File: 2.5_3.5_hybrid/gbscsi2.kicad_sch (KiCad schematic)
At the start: 120 parts, among them J1 Conn_01x02, J2 TF003, J4 Conn_01x04, J5 SCSI_50-2P_2mm, J6 SCSI_50P_2.54mm, Q1 AO3401A, Q10 AO3401A, Q11 AO3401A, Q12 AO3401A, Q13 AO3401A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

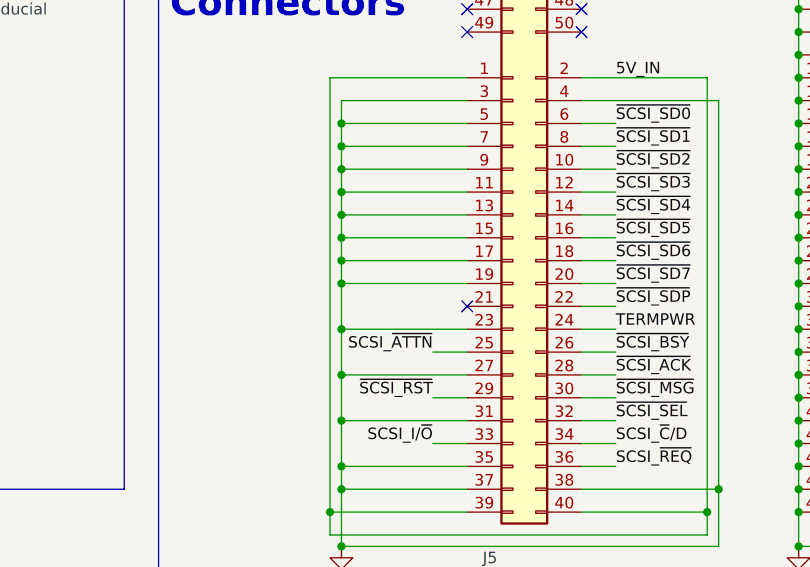
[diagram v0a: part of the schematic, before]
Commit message: Changed diodes in BoM, minor corrections to PCB, documentation
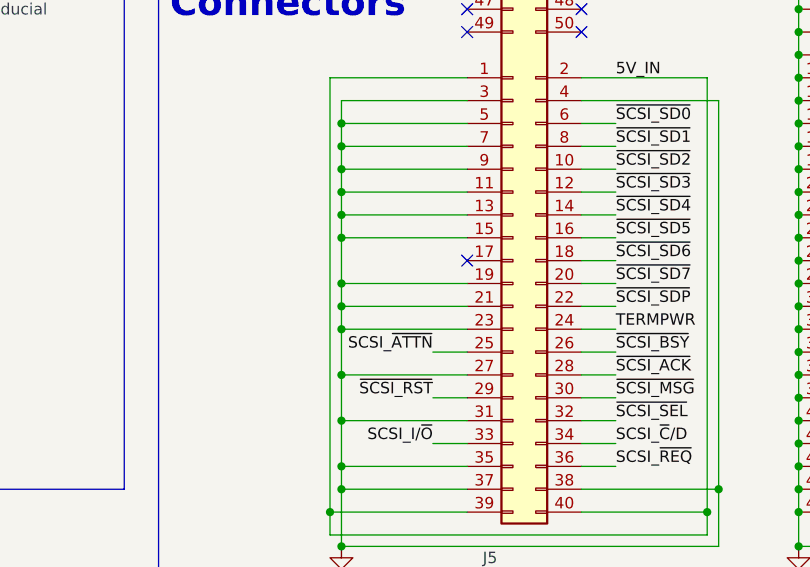
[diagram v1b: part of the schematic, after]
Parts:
- D? (x4): LCSC C8598 -> C82544
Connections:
- net GND: now also J5.21 (Pin_21); no longer J5.17 (Pin_17)
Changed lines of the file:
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@@
   (junction (at 187.96 77.47) (diameter 0) (color 0 0 0 0)
   )
+  (junction (at 320.04 57.15) (diameter 0) (color 0 0 0 0)
+  )
   (junction (at 384.81 59.69) (diameter 0) (color 0 0 0 0)
   )
@@
   (junction (at 328.93 158.75) (diameter 0) (color 0 0 0 0)
   )
-  (junction (at 320.04 52.07) (diameter 0) (color 0 0 0 0)
-  )
   (junction (at 370.84 77.47) (diameter 0) (color 0 0 0 0)
   )
@@
   (no_connect (at 346.71 21.59))
   (no_connect (at 54.61 77.47))
+  (no_connect (at 334.01 52.07))
   (no_connect (at 334.01 24.13))
   (no_connect (at 76.2 34.29))
   (no_connect (at 148.59 35.56))
-  (no_connect (at 334.01 57.15))
   (no_connect (at 334.01 21.59))
   (no_connect (at 76.2 31.75))
@@
     (stroke (width 0) (type default))
   )
+  (wire (pts (xy 320.04 57.15) (xy 334.01 57.15))
+    (stroke (width 0) (type default))
+  )
   (wire (pts (xy 370.84 49.53) (xy 370.84 52.07))
     (stroke (width 0) (type default))
@@
     (stroke (width 0) (type default))
   )
+  (wire (pts (xy 320.04 57.15) (xy 320.04 59.69))
+    (stroke (width 0) (type default))
+  )
   (wire (pts (xy 74.93 54.61) (xy 77.47 54.61))
     (stroke (width 0) (type default))
@@
     (stroke (width 0) (type default))
   )
-  (wire (pts (xy 320.04 52.07) (xy 334.01 52.07))
-    (stroke (width 0) (type default))
-  )
   (wire (pts (xy 193.04 200.66) (xy 193.04 198.12))
     (stroke (width 0) (type default))
@@
     (stroke (width 0) (type default))
   )
-  (wire (pts (xy 320.04 49.53) (xy 320.04 52.07))
-    (stroke (width 0) (type default))
-  )
   (wire (pts (xy 36.83 54.61) (xy 39.37 54.61))
     (stroke (width 0) (type default))
@@
     (stroke (width 0) (type default))
   )
-  (wire (pts (xy 320.04 52.07) (xy 320.04 54.61))
+  (wire (pts (xy 320.04 49.53) (xy 320.04 54.61))
     (stroke (width 0) (type default))
   )
-  (wire (pts (xy 320.04 54.61) (xy 320.04 59.69))
+  (wire (pts (xy 320.04 54.61) (xy 320.04 57.15))
     (stroke (width 0) (type default))
   )
@@
       (effects (font (size 1.27 1.27)))
     )
-    (property "LCSC" "C8598" (at 171.45 27.94 0)
+    (property "LCSC" "C82544" (at 171.45 27.94 0)
       (effects (font (size 1.27 1.27)) hide)
     )
@@
       (effects (font (size 1.27 1.27)))
     )
-    (property "LCSC" "C8598" (at 163.83 35.56 0)
+    (property "LCSC" "C82544" (at 163.83 35.56 0)
       (effects (font (size 1.27 1.27)) hide)
     )
@@
       (effects (font (size 1.27 1.27)))
     )
-    (property "LCSC" "C8598" (at 171.45 57.15 0)
+    (property "LCSC" "C82544" (at 171.45 57.15 0)
       (effects (font (size 1.27 1.27)) hide)
     )
@@
       (effects (font (size 1.27 1.27)))
     )
-    (property "LCSC" "C8598" (at 171.45 66.04 0)
+    (property "LCSC" "C82544" (at 171.45 66.04 0)
       (effects (font (size 1.27 1.27)) hide)
     )

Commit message: Cleaning up, updating docs
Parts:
- C1: value 100nF -> 10uF; LCSC C14663 -> C96446
- C? (x17): symbol zuluscsi-rescue:C_Small -> Device:C_Small
- D? (x4): symbol zuluscsi-rescue:D_Schottky -> Device:D_Schottky
- R? (x24): symbol zuluscsi-rescue:R -> Device:R
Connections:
- net +3V3 renamed +3.3V
